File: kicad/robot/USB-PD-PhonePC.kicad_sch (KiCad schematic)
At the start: 44 parts, among them U11 MAX77958EWV+T, U15 ESD122DMYR, U16 fpf1048bucx, U17 TPS61253AYFFR

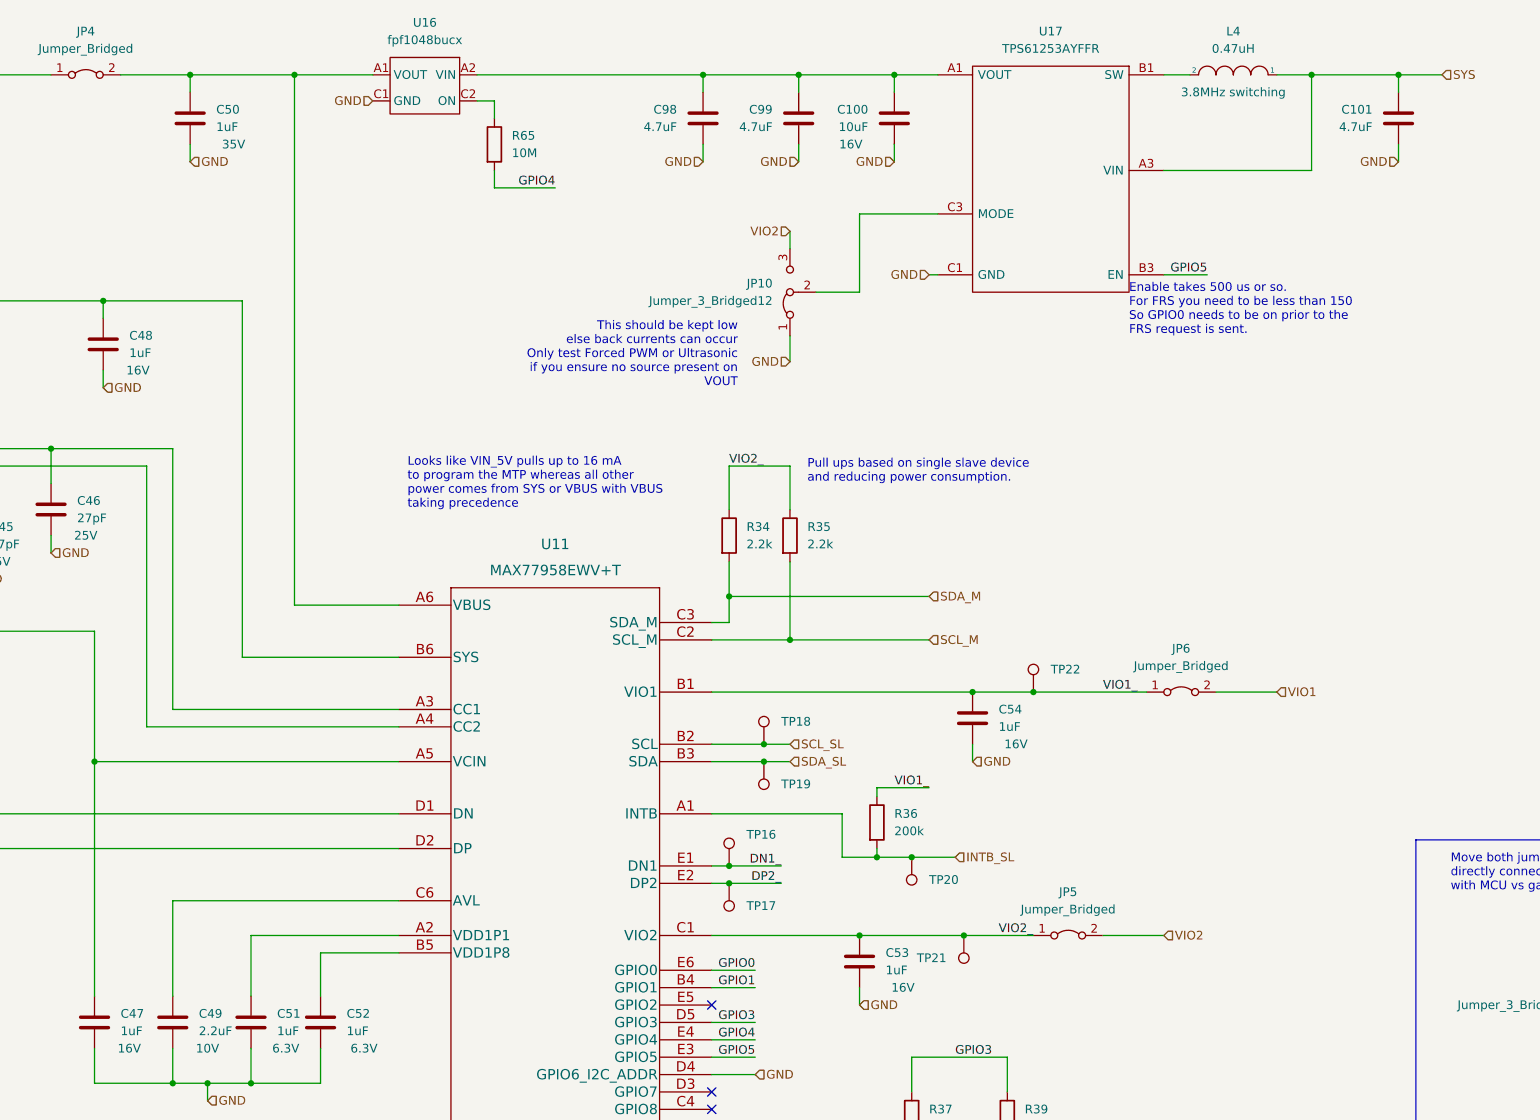
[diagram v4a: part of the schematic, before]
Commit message: Bulk capacitor field edits
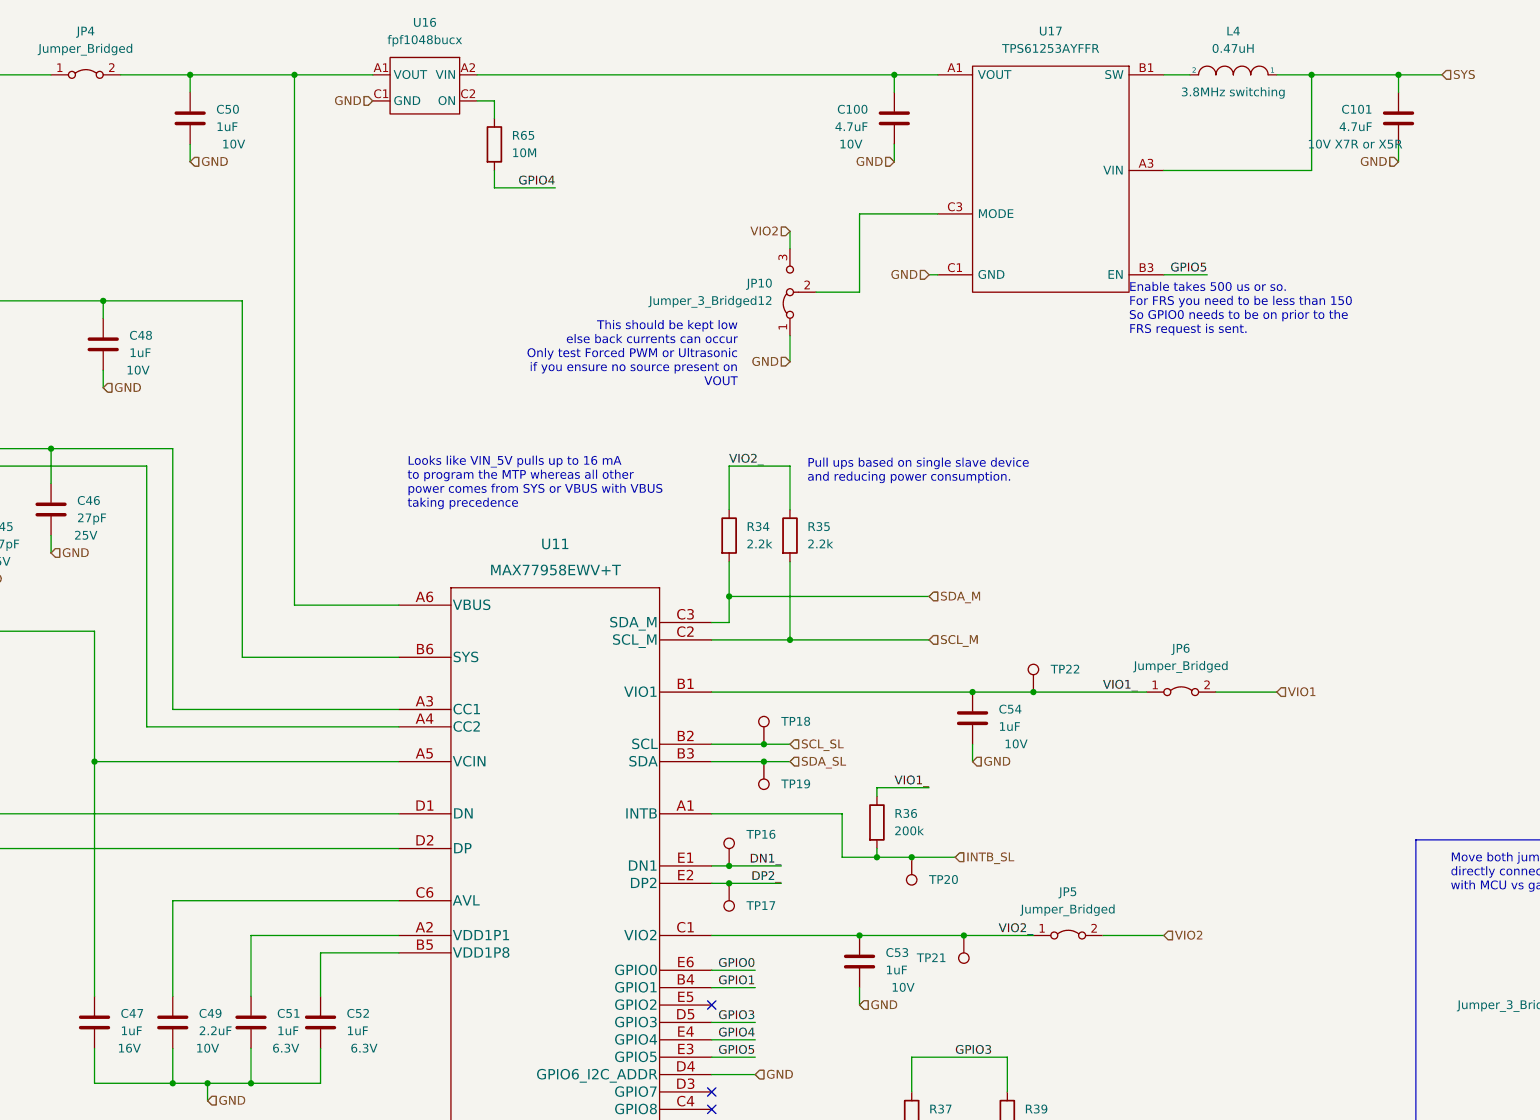
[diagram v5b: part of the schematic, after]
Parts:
- removed C98, C99: 4.7uF, Capacitor_SMD:C_0805_2012Metric, symbol Device:C
- C100: value 10uF -> 4.7uF; Manufacturer Samsung -> (none); Part Number CL21A106KOQNNNG -> (none)
- C101: Manufacturer Samsung -> (none); Part Number CL21A475KPFNNNE -> (none)
- C47, C48: Manufacturer Samsung -> (none); Part Number CL21B105KOFNNNE -> (none)
- C49: Manufacturer Samsung -> (none); Part Number CL10A225KP8NNNC -> (none)
- C50: Manufacturer Taiyo Yuden -> (none); Part Number GMK212BJ105KGHT -> (none)
- C51, C52: Manufacturer Samsung -> (none); Part Number CL10A105KQ8NNNC -> (none)
- C53, C54: Manufacturer Samsung -> (none); Part Number CL10A105KA8NNNC -> (none)
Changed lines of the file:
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@@
   (junction (at 287.02 293.37) (diameter 0) (color 0 0 0 0)
   )
-  (junction (at 322.58 120.65) (diameter 0) (color 0 0 0 0)
-  )
   (junction (at 185.42 233.68) (diameter 0) (color 0 0 0 0)
   )
   (junction (at 336.55 120.65) (diameter 0) (color 0 0 0 0)
-  )
-  (junction (at 308.61 120.65) (diameter 0) (color 0 0 0 0)
   )
   (junction (at 231.14 267.97) (diameter 0) (color 0 0 0 0)
@@
     (stroke (width 0) (type default) (color 0 0 0 0))
   )
-  (wire (pts (xy 322.58 130.81) (xy 322.58 133.35))
-    (stroke (width 0) (type default) (color 0 0 0 0))
-  )
   (wire (pts (xy 281.94 289.56) (xy 281.94 293.37))
     (stroke (width 0) (type default) (color 0 0 0 0))
   )
-  (wire (pts (xy 322.58 123.19) (xy 322.58 120.65))
-    (stroke (width 0) (type default) (color 0 0 0 0))
-  )
   (wire (pts (xy 341.63 224.79) (xy 334.01 224.79))
     (stroke (width 0) (type default) (color 0 0 0 0))
@@
     (stroke (width 0) (type default) (color 0 0 0 0))
   )
-  (wire (pts (xy 308.61 120.65) (xy 322.58 120.65))
-    (stroke (width 0) (type default) (color 0 0 0 0))
-  )
   (wire (pts (xy 248.92 120.65) (xy 260.35 120.65))
     (stroke (width 0) (type default) (color 0 0 0 0))
@@
     (stroke (width 0) (type default) (color 0 0 0 0))
   )
-  (wire (pts (xy 322.58 120.65) (xy 336.55 120.65))
+  (wire (pts (xy 275.59 120.65) (xy 336.55 120.65))
     (stroke (width 0) (type default) (color 0 0 0 0))
   )
@@
     (stroke (width 0) (type default) (color 0 0 0 0))
   )
-  (wire (pts (xy 308.61 130.81) (xy 308.61 133.35))
-    (stroke (width 0) (type default) (color 0 0 0 0))
-  )
-  (wire (pts (xy 308.61 123.19) (xy 308.61 120.65))
-    (stroke (width 0) (type default) (color 0 0 0 0))
-  )
   (polyline (pts (xy 412.75 284.48) (xy 457.2 284.48))
     (stroke (width 0) (type default) (color 0 0 0 0))
@@
   )
   (wire (pts (xy 312.42 238.76) (xy 320.04 238.76))
-    (stroke (width 0) (type default) (color 0 0 0 0))
-  )
-  (wire (pts (xy 275.59 120.65) (xy 308.61 120.65))
     (stroke (width 0) (type default) (color 0 0 0 0))
   )
@@
     (effects (font (size 1.27 1.27)) (justify right))
   )
-  (hierarchical_label "GND" (shape input) (at 322.58 133.35 180)
-    (effects (font (size 1.27 1.27)) (justify right))
-  )
   (hierarchical_label "INTB_SL" (shape input) (at 345.44 234.95 0)
     (effects (font (size 1.27 1.27)) (justify left))
@@
   )
   (hierarchical_label "GND" (shape input) (at 341.63 149.86 180)
-    (effects (font (size 1.27 1.27)) (justify right))
-  )
-  (hierarchical_label "GND" (shape input) (at 308.61 133.35 180)
     (effects (font (size 1.27 1.27)) (justify right))
   )
@@
       (effects (font (size 1.27 1.27)) hide)
     )
-    (property "Description" "16V" (id 4) (at 226.06 163.83 0))
-    (property "Manufacturer" "Samsung" (id 5) (at 220.98 160.02 0)
-      (effects (font (size 1.27 1.27)) hide)
-    )
-    (property "Part Number" "CL21B105KOFNNNE" (id 6) (at 220.98 160.02 0)
-      (effects (font (size 1.27 1.27)) hide)
-    )
+    (property "Description" "10V" (id 4) (at 226.06 163.83 0))
     (pin "1")
     (pin "2")
@@
     )
     (property "Description" "16V" (id 4) (at 224.79 262.89 0))
-    (property "Manufacturer" "Samsung" (id 5) (at 219.71 259.08 0)
-      (effects (font (size 1.27 1.27)) hide)
-    )
-    (property "Part Number" "CL21B105KOFNNNE" (id 6) (at 219.71 259.08 0)
+    (property "Manufacturer" "" (id 5) (at 219.71 259.08 0)
+      (effects (font (size 1.27 1.27)) hide)
+    )
+    (property "Part Number" "" (id 6) (at 219.71 259.08 0)
       (effects (font (size 1.27 1.27)) hide)
     )
@@
     )
     (property "Description" "10V" (id 4) (at 236.22 262.89 0))
-    (property "Manufacturer" "Samsung" (id 5) (at 231.14 259.08 0)
-      (effects (font (size 1.27 1.27)) hide)
-    )
-    (property "Part Number" "CL10A225KP8NNNC" (id 6) (at 231.14 259.08 0)
-      (effects (font (size 1.27 1.27)) hide)
-    )
     (pin "1")
     (pin "2")
@@
     )
     (property "Description" "6.3V" (id 4) (at 247.65 262.89 0))
-    (property "Manufacturer" "Samsung" (id 5) (at 242.57 259.08 0)
-      (effects (font (size 1.27 1.27)) hide)
-    )
-    (property "Part Number" "CL10A105KQ8NNNC" (id 6) (at 242.57 259.08 0)
-      (effects (font (size 1.27 1.27)) hide)
-    )
     (pin "1")
     (pin "2")
@@
     (pin "2")
   )
-  (symbol (lib_id "Device:C") (at 322.58 127 0) (mirror y) (unit 1)
-    (in_bom yes) (on_board yes)
-    (property "Reference" "C99" (id 0) (at 318.77 125.7299 0)
-      (effects (font (size 1.27 1.27)) (justify left))
-    )
-    (property "Value" "4.7uF" (id 1) (at 318.77 128.2699 0)
-      (effects (font (size 1.27 1.27)) (justify left))
-    )
-    (property "Footprint" "Capacitor_SMD:C_0805_2012Metric" (id 2) (at 321.6148 130.81 0)
-      (effects (font (size 1.27 1.27)) hide)
-    )
-    (property "Datasheet" "~" (id 3) (at 322.58 127 0)
-      (effects (font (size 1.27 1.27)) hide)
-    )
-    (property "Description" "" (id 4) (at 316.23 130.81 0))
-    (property "Manufacturer" "Samsung" (id 5) (at 322.58 127 0)
-      (effects (font (size 1.27 1.27)) hide)
-    )
-    (property "Part Number" "CL21A475KPFNNNE" (id 6) (at 322.58 127 0)
-      (effects (font (size 1.27 1.27)) hide)
-    )
-    (pin "1")
-    (pin "2")
-  )
   (symbol (lib_id "Device:C") (at 252.73 259.08 0) (unit 1)
     (in_bom yes) (on_board yes)
@@
     )
     (property "Description" "6.3V" (id 4) (at 259.08 262.89 0))
-    (property "Manufacturer" "Samsung" (id 5) (at 252.73 259.08 0)
-      (effects (font (size 1.27 1.27)) hide)
-    )
-    (property "Part Number" "CL10A105KQ8NNNC" (id 6) (at 252.73 259.08 0)
-      (effects (font (size 1.27 1.27)) hide)
-    )
     (pin "1")
     (pin "2")
@@
       (effects (font (size 1.27 1.27)) hide)
     )
-    (property "Description" "35V" (id 4) (at 240.03 130.81 0))
-    (property "Manufacturer" "Taiyo Yuden" (id 5) (at 233.68 127 0)
-      (effects (font (size 1.27 1.27)) hide)
-    )
-    (property "Part Number" "GMK212BJ105KGHT" (id 6) (at 233.68 127 0)
-      (effects (font (size 1.27 1.27)) hide)
-    )
+    (property "Description" "10V" (id 4) (at 240.03 130.81 0))
     (pin "1")
     (pin "2")
@@
       (effects (font (size 1.27 1.27)) hide)
     )
-    (property "Description" "" (id 4) (at 403.86 130.81 0))
-    (property "Manufacturer" "Samsung" (id 5) (at 410.21 127 0)
-      (effects (font (size 1.27 1.27)) hide)
-    )
-    (property "Part Number" "CL21A475KPFNNNE" (id 6) (at 410.21 127 0)
-      (effects (font (size 1.27 1.27)) hide)
-    )
+    (property "Description" "10V X7R or X5R" (id 4) (at 403.86 130.81 0))
     (pin "1")
     (pin "2")
@@
       (effects (font (size 1.27 1.27)) (justify left))
     )
-    (property "Value" "10uF" (id 1) (at 332.74 128.2699 0)
+    (property "Value" "4.7uF" (id 1) (at 332.74 128.2699 0)
       (effects (font (size 1.27 1.27)) (justify left))
     )
@@
       (effects (font (size 1.27 1.27)) hide)
     )
-    (property "Description" "16V" (id 4) (at 330.2 130.81 0))
-    (property "Manufacturer" "Samsung" (id 5) (at 336.55 127 0)
-      (effects (font (size 1.27 1.27)) hide)
-    )
-    (property "Part Number" "CL21A106KOQNNNG" (id 6) (at 336.55 127 0)
-      (effects (font (size 1.27 1.27)) hide)
-    )
+    (property "Description" "10V" (id 4) (at 330.2 130.81 0))
     (pin "1")
     (pin "2")
@@
       (effects (font (size 1.27 1.27)) hide)
     )
-    (property "Description" "16V" (id 4) (at 337.82 254 0))
-    (property "Manufacturer" "Samsung" (id 5) (at 331.47 250.19 0)
-      (effects (font (size 1.27 1.27)) hide)
-    )
-    (property "Part Number" "CL10A105KA8NNNC" (id 6) (at 331.47 250.19 0)
-      (effects (font (size 1.27 1.27)) hide)
-    )
+    (property "Description" "10V" (id 4) (at 337.82 254 0))
     (pin "1")
     (pin "2")
@@
       (effects (font (size 1.27 1.27)) hide)
     )
-    (property "Description" "16V" (id 4) (at 354.33 218.44 0))
-    (property "Manufacturer" "Samsung" (id 5) (at 347.98 214.63 0)
-      (effects (font (size 1.27 1.27)) hide)
-    )
-    (property "Part Number" "CL10A105KA8NNNC" (id 6) (at 347.98 214.63 0)
-      (effects (font (size 1.27 1.27)) hide)
-    )
-    (pin "1")
-    (pin "2")
-  )
-  (symbol (lib_id "Device:C") (at 308.61 127 0) (mirror y) (unit 1)
-    (in_bom yes) (on_board yes)
-    (property "Reference" "C98" (id 0) (at 304.8 125.7299 0)
-      (effects (font (size 1.27 1.27)) (justify left))
-    )
-    (property "Value" "4.7uF" (id 1) (at 304.8 128.2699 0)
-      (effects (font (size 1.27 1.27)) (justify left))
-    )
-    (property "Footprint" "Capacitor_SMD:C_0805_2012Metric" (id 2) (at 307.6448 130.81 0)
-      (effects (font (size 1.27 1.27)) hide)
-    )
-    (property "Datasheet" "~" (id 3) (at 308.61 127 0)
-      (effects (font (size 1.27 1.27)) hide)
-    )
-    (property "Description" "" (id 4) (at 302.26 130.81 0))
-    (property "Manufacturer" "Samsung" (id 5) (at 308.61 127 0)
-      (effects (font (size 1.27 1.27)) hide)
-    )
-    (property "Part Number" "CL21A475KPFNNNE" (id 6) (at 308.61 127 0)
-      (effects (font (size 1.27 1.27)) hide)
-    )
-    (pin "1")
-    (pin "2")
+    (property "Description" "10V" (id 4) (at 354.33 218.44 0))
+    (pin "1")
+    (pin "2")

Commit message: bulk footprint updates to capacitors
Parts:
- C47, C48, C50: footprint Capacitor_SMD:C_0805_2012Metric -> Capacitor_SMD:C_0402_1005Metric
- C51, C52, C53, C54: footprint Capacitor_SMD:C_0603_1608Metric -> Capacitor_SMD:C_0402_1005Metric
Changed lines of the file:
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@@
       (effects (font (size 1.27 1.27)) (justify left))
     )
-    (property "Footprint" "Capacitor_SMD:C_0805_2012Metric" (id 2) (at 221.9452 163.83 0)
+    (property "Footprint" "Capacitor_SMD:C_0402_1005Metric" (id 2) (at 221.9452 163.83 0)
       (effects (font (size 1.27 1.27)) hide)
     )
@@
       (effects (font (size 1.27 1.27)) (justify left))
     )
-    (property "Footprint" "Capacitor_SMD:C_0805_2012Metric" (id 2) (at 220.6752 262.89 0)
+    (property "Footprint" "Capacitor_SMD:C_0402_1005Metric" (id 2) (at 220.6752 262.89 0)
       (effects (font (size 1.27 1.27)) hide)
     )
@@
       (effects (font (size 1.27 1.27)) (justify left))
     )
-    (property "Footprint" "Capacitor_SMD:C_0603_1608Metric" (id 2) (at 243.5352 262.89 0)
+    (property "Footprint" "Capacitor_SMD:C_0402_1005Metric" (id 2) (at 243.5352 262.89 0)
       (effects (font (size 1.27 1.27)) hide)
     )
@@
       (effects (font (size 1.27 1.27)) (justify left))
     )
-    (property "Footprint" "Capacitor_SMD:C_0603_1608Metric" (id 2) (at 253.6952 262.89 0)
+    (property "Footprint" "Capacitor_SMD:C_0402_1005Metric" (id 2) (at 253.6952 262.89 0)
       (effects (font (size 1.27 1.27)) hide)
     )
@@
       (effects (font (size 1.27 1.27)) (justify left))
     )
-    (property "Footprint" "Capacitor_SMD:C_0805_2012Metric" (id 2) (at 234.6452 130.81 0)
+    (property "Footprint" "Capacitor_SMD:C_0402_1005Metric" (id 2) (at 234.6452 130.81 0)
       (effects (font (size 1.27 1.27)) hide)
     )
@@
       (effects (font (size 1.27 1.27)) (justify left))
     )
-    (property "Footprint" "Capacitor_SMD:C_0603_1608Metric" (id 2) (at 332.4352 254 0)
+    (property "Footprint" "Capacitor_SMD:C_0402_1005Metric" (id 2) (at 332.4352 254 0)
       (effects (font (size 1.27 1.27)) hide)
     )
@@
       (effects (font (size 1.27 1.27)) (justify left))
     )
-    (property "Footprint" "Capacitor_SMD:C_0603_1608Metric" (id 2) (at 348.9452 218.44 0)
-      (effects (font (size 1.27 1.27)) hide)
-    )
+    (property "Footprint" "Capacitor_SMD:C_0402_1005Metric" (id 2) (at 348.9452 218.44 0)
+      (effects (font (size 1.27 1.27)) hide)
+    )

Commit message: Moved usb-c-phonepc into USB-PD-PhonePC and fixed inverted dn/dp pins
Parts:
- added C97: 4.7uF, Capacitor_SMD:C_0805_2012Metric, symbol Device:C
- added D3: PTVS20VS1UR, Diode_SMD:Nexperia_CFP3_SOD-123W, symbol Device:D_Zener
- added J4: USB4120-03-C_REVA, Connector_USB:GCT_USB4120-03-C_REVA, symbol Connector:USB4120-03-C_REVA
- added TP13, TP14, TP15, TP29, TP30: TP5002, TestPoint:KEYSTONE_5002, symbol Connector:TestPoint
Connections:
- net GND: now also C97.2, D3.2 (A), J4.A1 (GND), J4.A12 (GND), J4.B1 (GND), J4.B12 (GND), J4.SHELL; no longer C45.2, C46.2, C47.2, C49.2, C51.2, C52.2, C53.2, C54.2, JP10.1 (A), U11.C5 (GND_A), U11.D4 (GPIO6), U11.D6 (GND_D)
- net CC1: no longer names the net of C46.1, U11.A3 (CC1)
- net CC1: now also J4.A5 (CC1), TP15.1
- net CC2: no longer names the net of C45.1, U11.A4 (CC2)
- net CC2: now also J4.B5 (CC2), TP29.1
- net DN renamed DN_EXT
- net DN_EXT: now also J4.A7 (Dn1), J4.B7 (Dn2), TP13.1
- net DN1_ renamed DN_Switched
- net DP renamed DP_EXT
- net DP_EXT: now also J4.A6 (Dp1), J4.B6 (Dp2), TP14.1
- net DP2_ renamed DP2_Switched
- net SBU1: no longer names the net of R38.2
- net SBU1: now also J4.A8 (SBU1)
- net SBU2: no longer names the net of R40.2
- net SBU2: now also J4.B8 (SBU2)
- net VBUS: no longer names the net of JP4.1 (A)
- net VBUS: now also C97.1, D3.1 (K), J4.A4 (VBUS), J4.A9 (VBUS), J4.B4 (VBUS), J4.B9 (VBUS), TP30.1
- new net AGND: C45.2, C46.2, C47.2, C49.2, C51.2, C52.2, C53.2, C54.2, JP10.1 (A), U11.C5 (GND_A), U11.D4 (GPIO6), U11.D6 (GND_D)
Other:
- moved on the sheet: R37, R38, R39, R40
